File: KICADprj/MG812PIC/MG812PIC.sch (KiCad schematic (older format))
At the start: 6 parts, among them IC1 PIC16F18326-I_P, J1 AE-CH340E-TYPEC, J2 Conn_01x06

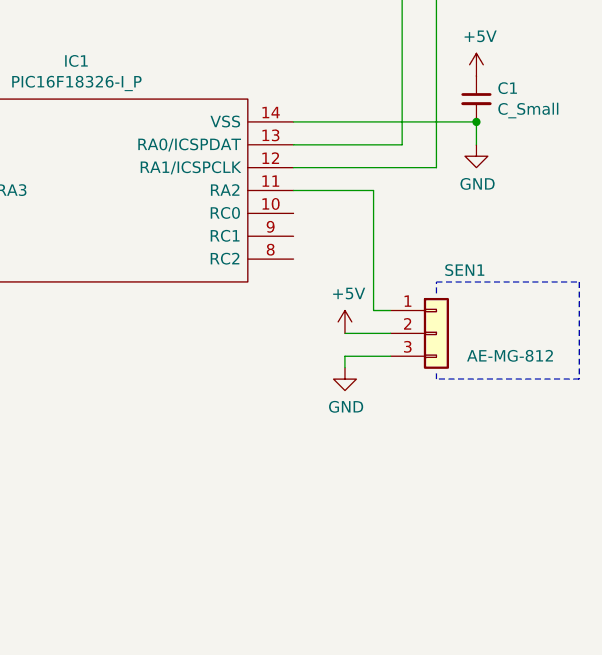
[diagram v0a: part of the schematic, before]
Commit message: マニュアルキャリブレーション追加
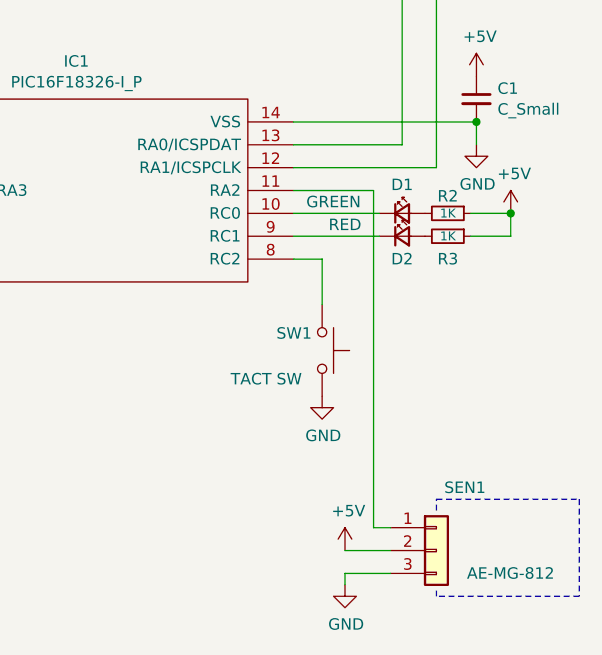
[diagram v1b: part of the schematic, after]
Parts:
- added D1: GREEN, symbol Device:LED_Small
- added D2: RED, symbol Device:LED_Small
- added R2, R3: 1K, symbol Device:R_Small
- added SW1: TACT SW, symbol Switch:SW_MEC_5G
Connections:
- net +5V: now also R2.1, R3.1
- net GND: now also SW1.3 (B), SW1.4 (B)
- net at IC1.10 (RC0): now also D1.1 (K)
- net at IC1.8 (RC2): now also SW1.1 (A), SW1.2 (A)
- net at IC1.9 (RC1): now also D2.1 (K)
- new net: D1.2 (A), R2.2
- new net: D2.2 (A), R3.2
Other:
- moved on the sheet: SEN1
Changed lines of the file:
@@
 encoding utf-8
 Sheet 1 1
-Title "MG812-PIC"
+Title "MG812-PIC USB-SERIAL demo"
 Date "2022-07-17"
 Rev ""
-Comp "USB-SERIAL demo"
+Comp ""
 Comment1 ""
 Comment2 ""
@@
 L Connector_Generic:Conn_01x03 SEN?
 U 1 1 62D41E24
-P 6925 4625
+P 6925 5575
 AR Path="/62D3A28E/62D41E24" Ref="SEN?"  Part="1"
 AR Path="/62D41E24" Ref="SEN1"  Part="1"
-F 0 "SEN1" H 7050 4900 50  0000 C CNN
-F 1 "AE-MG-812" H 7250 4525 50  0000 C CNN
-F 2 "" H 6925 4625 50  0001 C CNN
-F 3 "~" H 6925 4625 50  0001 C CNN
-	1    6925 4625
+F 0 "SEN1" H 7050 5850 50  0000 C CNN
+F 1 "AE-MG-812" H 7250 5475 50  0000 C CNN
+F 2 "" H 6925 5575 50  0001 C CNN
+F 3 "~" H 6925 5575 50  0001 C CNN
+	1    6925 5575
 	1    0    0    -1
 $EndComp
@@
 L power:+5V #PWR?
 U 1 1 62D41E2A
-P 6525 4625
+P 6525 5575
 AR Path="/62D3A28E/62D41E2A" Ref="#PWR?"  Part="1"
 AR Path="/62D41E2A" Ref="#PWR06"  Part="1"
-F 0 "#PWR06" H 6525 4475 50  0001 C CNN
-F 1 "+5V" H 6540 4798 50  0000 C CNN
-F 2 "" H 6525 4625 50  0001 C CNN
-F 3 "" H 6525 4625 50  0001 C CNN
-	1    6525 4625
+F 0 "#PWR06" H 6525 5425 50  0001 C CNN
+F 1 "+5V" H 6540 5748 50  0000 C CNN
+F 2 "" H 6525 5575 50  0001 C CNN
+F 3 "" H 6525 5575 50  0001 C CNN
+	1    6525 5575
 	1    0    0    -1
 $EndComp
@@
 L power:GND #PWR?
 U 1 1 62D41E30
-P 6525 4775
+P 6525 5725
 AR Path="/62D3A28E/62D41E30" Ref="#PWR?"  Part="1"
 AR Path="/62D41E30" Ref="#PWR07"  Part="1"
-F 0 "#PWR07" H 6525 4525 50  0001 C CNN
-F 1 "GND" H 6530 4602 50  0000 C CNN
-F 2 "" H 6525 4775 50  0001 C CNN
-F 3 "" H 6525 4775 50  0001 C CNN
-	1    6525 4775
-	1    0    0    -1
-$EndComp
-Wire Wire Line
-	6725 4725 6525 4725
-Wire Wire Line
-	6525 4725 6525 4775
-Wire Wire Line
-	6725 4625 6525 4625
+F 0 "#PWR07" H 6525 5475 50  0001 C CNN
+F 1 "GND" H 6530 5552 50  0000 C CNN
+F 2 "" H 6525 5725 50  0001 C CNN
+F 3 "" H 6525 5725 50  0001 C CNN
+	1    6525 5725
+	1    0    0    -1
+$EndComp
+Wire Wire Line
+	6725 5675 6525 5675
+Wire Wire Line
+	6525 5675 6525 5725
+Wire Wire Line
+	6725 5575 6525 5575
 Wire Wire Line
 	6300 4000 6650 4000
 Wire Wire Line
-	6650 4000 6650 4525
-Wire Wire Line
-	6650 4525 6725 4525
+	6650 4000 6650 5475
+Wire Wire Line
+	6650 5475 6725 5475
 $Comp
 L Connector_Generic:Conn_01x06 J?
@@
 $EndComp
 Wire Notes Line
-	6925 4450 6925 4400
-Wire Notes Line
-	6925 4400 7550 4400
-Wire Notes Line
-	7550 4400 7550 4825
-Wire Notes Line
-	7550 4825 6925 4825
-Wire Notes Line
-	6925 4825 6925 4800
+	6925 5400 6925 5350
+Wire Notes Line
+	6925 5350 7550 5350
+Wire Notes Line
+	7550 5350 7550 5775
+Wire Notes Line
+	7550 5775 6925 5775
+Wire Notes Line
+	6925 5775 6925 5750
 Wire Notes Line
 	3700 4375 3700 4325
@@
 	1    0    0    -1
 $EndComp
+$Comp
+L Switch:SW_MEC_5G SW1
+U 1 1 62D4D13D
+P 6425 4700
+F 0 "SW1" V 6350 4500 50  0000 L CNN
+F 1 "TACT SW" V 6550 4300 50  0000 L CNN
+F 2 "" H 6425 4900 50  0001 C CNN
+F 3 "http://www.apem.com/int/index.php?controller=attachment&id_attachment=488" H 6425 4900 50  0001 C CNN
+	1    6425 4700
+	0    1    1    0
+$EndComp
+Wire Wire Line
+	6300 4300 6425 4300
+Wire Wire Line
+	6425 4300 6425 4500
+$Comp
+L power:GND #PWR?
+U 1 1 62D4EEA2
+P 6425 4900
+AR Path="/62D3A28E/62D4EEA2" Ref="#PWR?"  Part="1"
+AR Path="/62D4EEA2" Ref="#PWR011"  Part="1"
+F 0 "#PWR011" H 6425 4650 50  0001 C CNN
+F 1 "GND" H 6430 4727 50  0000 C CNN
+F 2 "" H 6425 4900 50  0001 C CNN
+F 3 "" H 6425 4900 50  0001 C CNN
+	1    6425 4900
+	1    0    0    -1
+$EndComp
+$Comp
+L Device:LED_Small D1
+U 1 1 62D4BD1D
+P 6775 4100
+F 0 "D1" H 6775 4225 50  0000 C CNN
+F 1 "GREEN" H 6475 4150 50  0000 C CNN
+F 2 "" V 6775 4100 50  0001 C CNN
+F 3 "~" V 6775 4100 50  0001 C CNN
+	1    6775 4100
+	1    0    0    -1
+$EndComp
+$Comp
+L Device:LED_Small D2
+U 1 1 62D4C7DA
+P 6775 4200
+F 0 "D2" H 6775 4100 50  0000 C CNN
+F 1 "RED" H 6525 4250 50  0000 C CNN
+F 2 "" V 6775 4200 50  0001 C CNN
+F 3 "~" V 6775 4200 50  0001 C CNN
+	1    6775 4200
+	1    0    0    -1
+$EndComp
+Wire Wire Line
+	6300 4100 6675 4100
+Wire Wire Line
+	6675 4200 6300 4200
+$Comp
+L Device:R_Small R3
+U 1 1 62D537AD
+P 6975 4200
+F 0 "R3" V 7075 4200 50  0000 C CNN
+F 1 "1K" V 6975 4200 39  0000 C CNN
+F 2 "" H 6975 4200 50  0001 C CNN
+F 3 "~" H 6975 4200 50  0001 C CNN
+	1    6975 4200
+	0    1    1    0
+$EndComp
+$Comp
+L Device:R_Small R2
+U 1 1 62D53C7C
+P 6975 4100
+F 0 "R2" V 6900 4100 50  0000 C CNN
+F 1 "1K" V 6975 4100 39  0000 C CNN
+F 2 "" H 6975 4100 50  0001 C CNN
+F 3 "~" H 6975 4100 50  0001 C CNN
+	1    6975 4100
+	0    1    1    0
+$EndComp
+$Comp
+L power:+5V #PWR?
+U 1 1 62D5A6B6
+P 7250 4100
+AR Path="/62D3A28E/62D5A6B6" Ref="#PWR?"  Part="1"
+AR Path="/62D5A6B6" Ref="#PWR012"  Part="1"
+F 0 "#PWR012" H 7250 3950 50  0001 C CNN
+F 1 "+5V" H 7265 4273 50  0000 C CNN
+F 2 "" H 7250 4100 50  0001 C CNN
+F 3 "" H 7250 4100 50  0001 C CNN
+	1    7250 4100
+	1    0    0    -1
+$EndComp
+Wire Wire Line
+	7075 4100 7250 4100
+Wire Wire Line
+	7075 4200 7250 4200
+Wire Wire Line
+	7250 4200 7250 4100
+Connection ~ 7250 4100
 $EndSCHEMATC
